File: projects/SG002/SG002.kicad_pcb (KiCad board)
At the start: 2 copper layers, 53.1 x 82.6 mm, 31 parts, among them J1 Conn_01x04, J2 Conn_01x02, J3 Conn_01x06, M31 MOUNTHOLE_M3, M32 MOUNTHOLE_M3, M33 MOUNTHOLE_M3, M34 MOUNTHOLE_M3, U1 74HC595N, U2 74HC595N, U3 74HC595N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

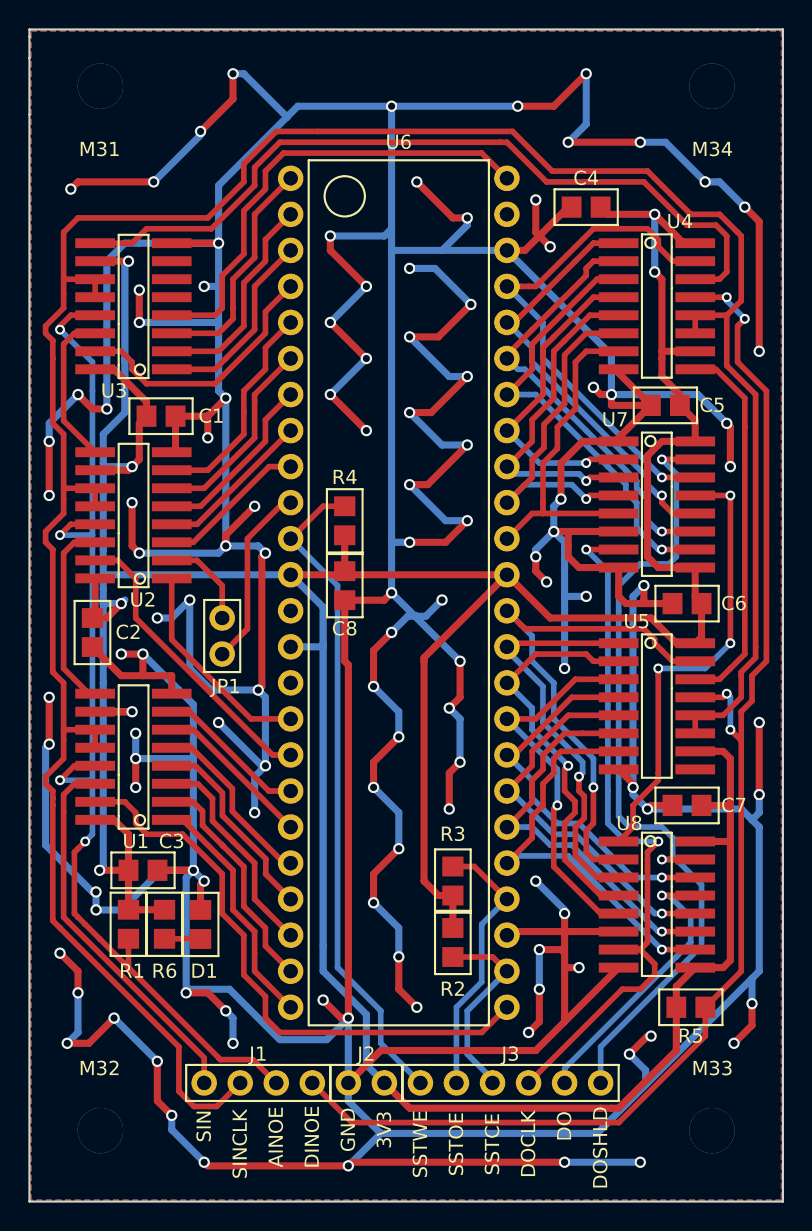
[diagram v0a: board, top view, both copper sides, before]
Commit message: SG002 completed and gerbers released as SG002P1.
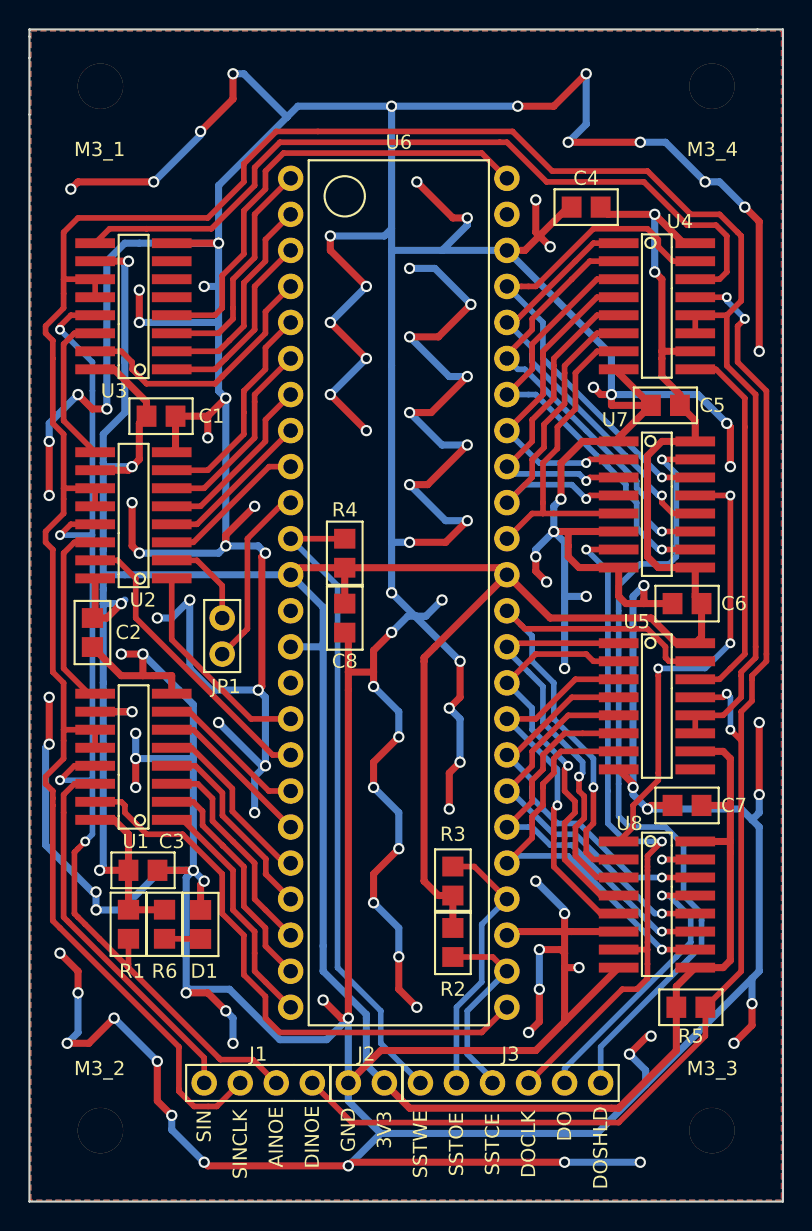
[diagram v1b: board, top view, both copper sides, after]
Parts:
- moved C8 2.29 mm to (109.2, 90.9)
- moved R4 2.29 mm to (109.2, 86.4)
- renumbered M31 to M3_1, M32 to M3_2, M33 to M3_3, M34 to M3_4
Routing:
- net GND_: track 803.6 -> 799.5 mm
- net /D4: track 24.1 -> 23.1 mm
- net /D12: track 26.0 -> 25.0 mm
- net /SST_WE: track 46.9 -> 46.0 mm
- net /DATA_OUT_SHLD: track 59.6 -> 60.3 mm
- net +3V3_: track 303.3 -> 302.7 mm
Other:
- rule pad_to_mask_clearance: 0.2 -> 0.1
